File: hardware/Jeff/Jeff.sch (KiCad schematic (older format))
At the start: 1 part

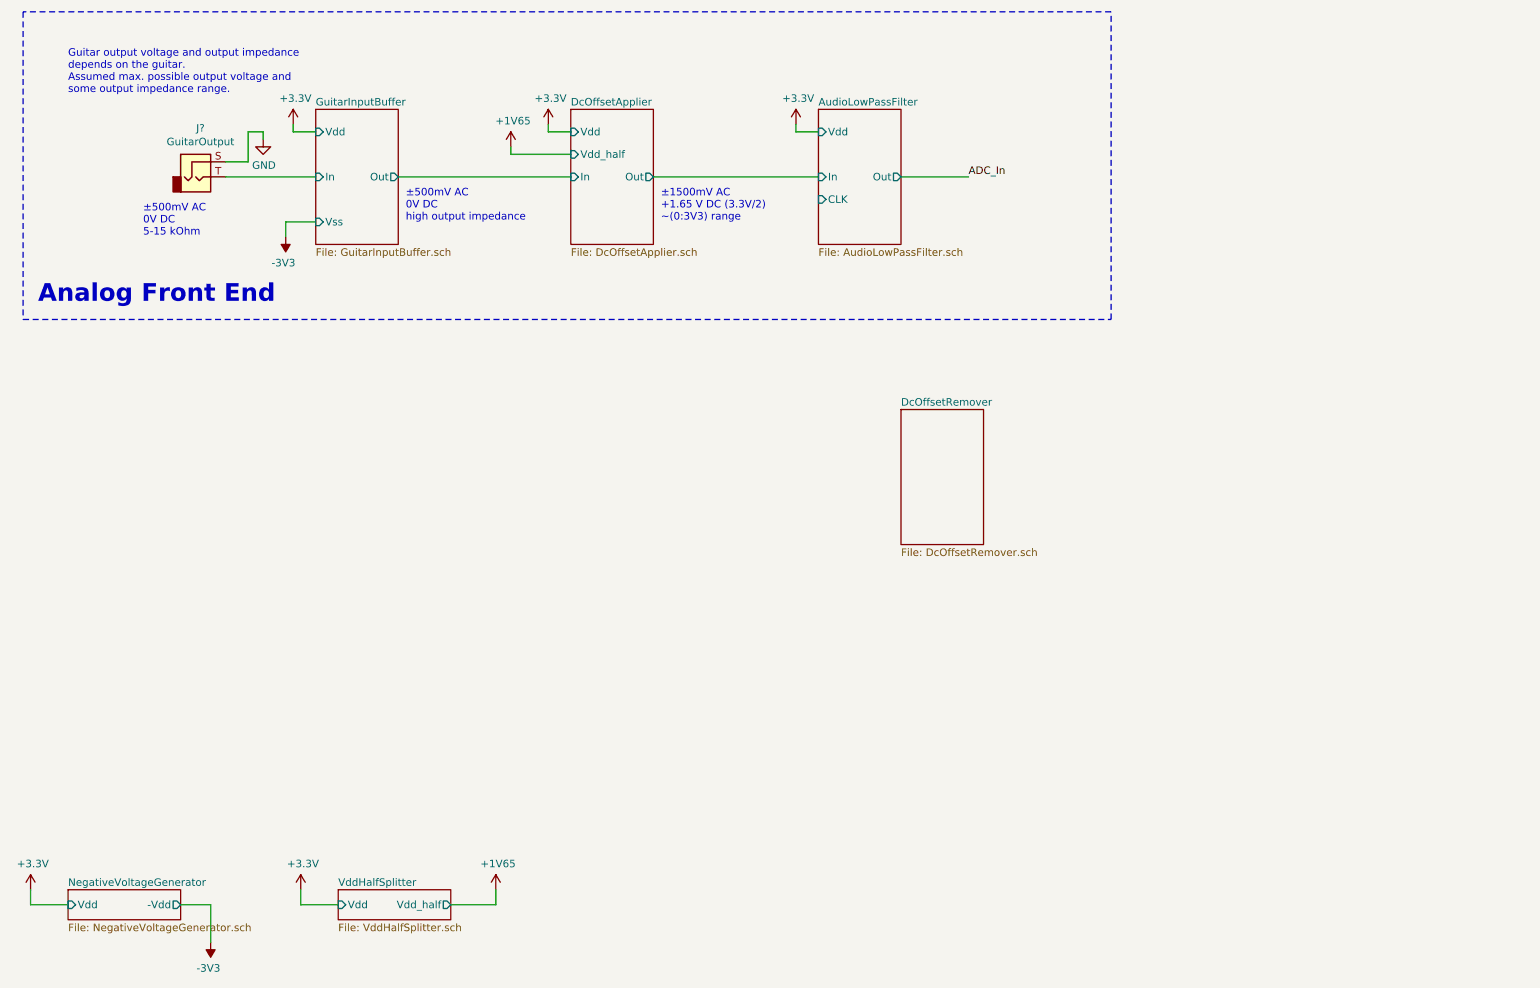
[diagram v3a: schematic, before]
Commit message: Add DSP block and connect to analog front end
The DSP block contains STM32L432KC nucleo board, which is also added
with this commit, as a library. The output of the analog front end has
been connected to the CPU as well as the cutoff frequency setter clock.
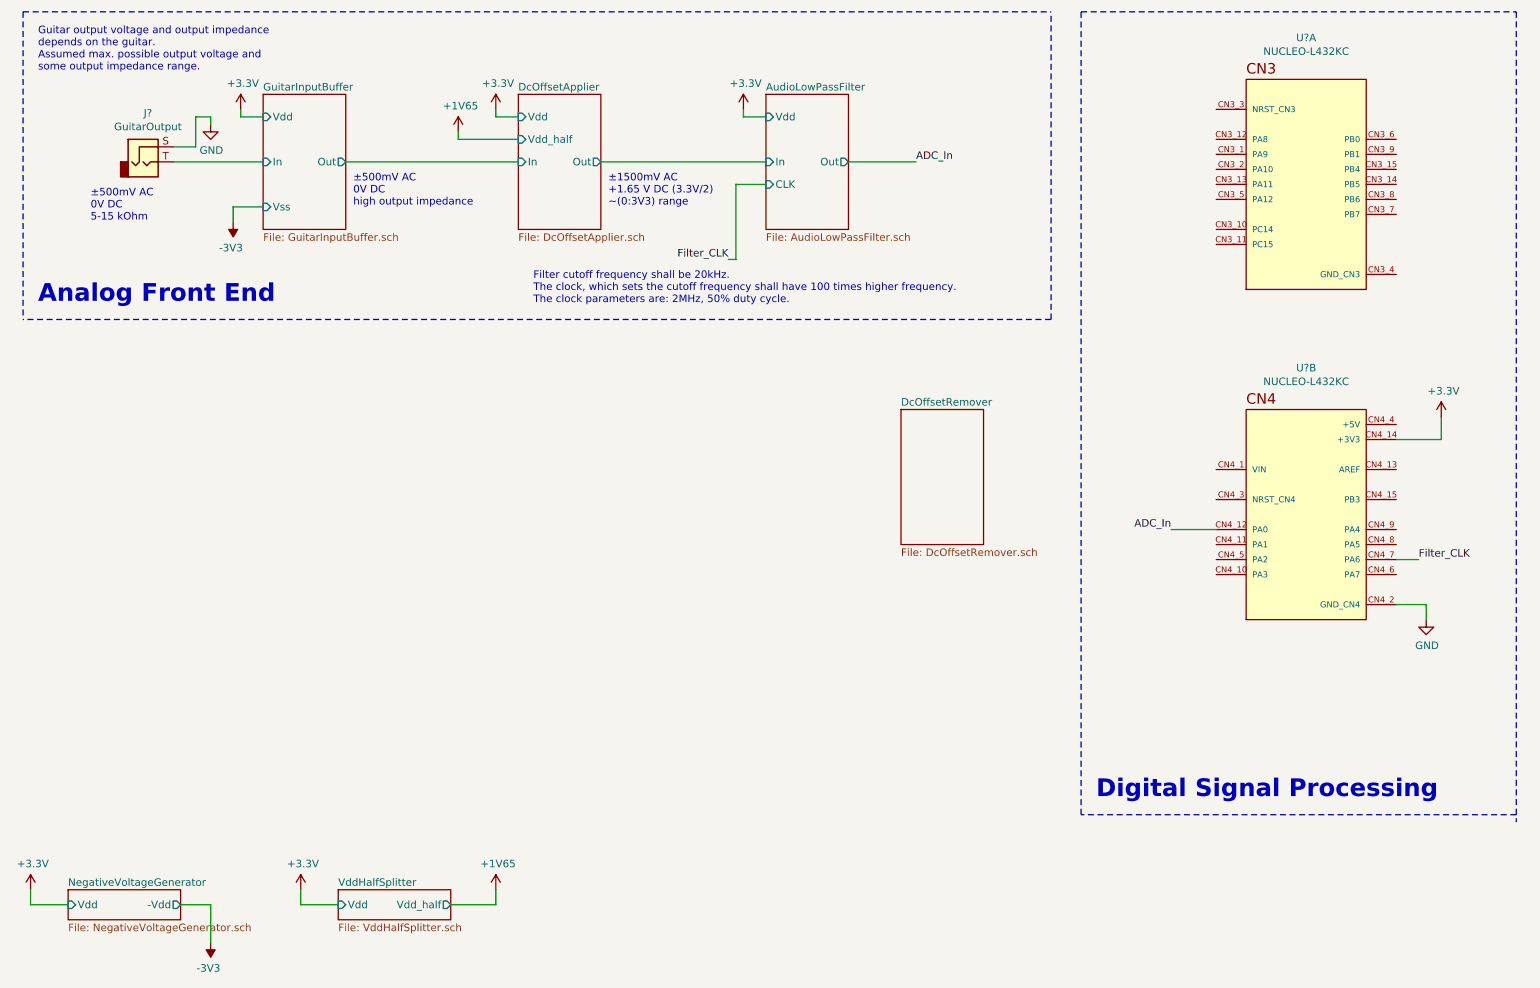
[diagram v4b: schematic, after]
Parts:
- added U? (x2): NUCLEO-L432KC, MODULE_NUCLEO-L432KC, symbol Nucleo-L432KC:NUCLEO-L432KC
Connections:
- net +3V3: now also U?.CN4_14 (+3V3)
- net ADC_In: now also U?.CN4_12 (PA0)
- net GND: now also U?.CN4_2 (GND_CN4)
- new net Filter_CLK: U?.CN4_7 (PA6)
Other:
- note added: "Digital Signal Processing"
- note added: "Filter cutoff frequency shall be 20kHz.\nThe clock, which sets the cutoff frequency shall have 100 times higher frequency.\nThe clock parameters are: 2MHz, 50% duty cycle."
- moved on the sheet: J?

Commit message: Add Post-DAC stage schematic
This includes the low pass filter, which is the same like the one in the
Front End, the offset remover circuit, all the connections to DSP stage,
which is the DAC output and the filter cutoff setter clock.
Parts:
- added J?: JeffOutput, symbol Connector:AudioJack2
- J?: value GuitarOutput -> Guitar
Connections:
- net GND: now also J?.S
- net DAC_Out: now reaches U?.CN4_9 (PA4)
- new net DcOffsetRemover/Out: J?.T
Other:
- note added: "Miscellanuous"
- note added: "Post-DAC Stage"
- note added: "±1650mV AC\n0V DC"
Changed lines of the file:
@@
 $Descr A4 11693 8268
 encoding utf-8
-Sheet 1 7
+Sheet 1 8
 Title ""
 Date ""
@@
 P 1800 1800
 F 0 "J?" H 1832 2125 50  0000 C CNN
-F 1 "GuitarOutput" H 1832 2034 50  0000 C CNN
+F 1 "Guitar" H 1832 2034 50  0000 C CNN
 F 2 "" H 1800 1800 50  0001 C CNN
 F 3 "~" H 1800 1800 50  0001 C CNN
@@
 Wire Wire Line
 	2250 1500 2150 1500
-$Sheet
-S 6850 3450 550  900
-U 6216C0D1
-F0 "DcOffsetRemover" 50
-F1 "DcOffsetRemover.sch" 50
-$EndSheet
 Text Notes 1450 2200 0    50   ~ 0
 ±500mV AC\n0V DC\n5-15 kOhm
@@
 	5800 1500 5800 1450
 $Sheet
-S 1300 6650 750  200
+S 2100 6000 750  200
 U 6219438A
 F0 "NegativeVoltageGenerator" 50
 F1 "NegativeVoltageGenerator.sch" 50
-F2 "Vdd" I L 1300 6750 50
-F3 "-Vdd" O R 2050 6750 50
+F2 "Vdd" I L 2100 6100 50
+F3 "-Vdd" O R 2850 6100 50
 $EndSheet
 $Comp
 L power:+3.3V #PWR?
 U 1 1 6219F15D
-P 1050 6650
-F 0 "#PWR?" H 1050 6500 50  0001 C CNN
-F 1 "+3.3V" H 1065 6823 50  0000 C CNN
-F 2 "" H 1050 6650 50  0001 C CNN
-F 3 "" H 1050 6650 50  0001 C CNN
-	1    1050 6650
-	1    0    0    -1
-$EndComp
-Wire Wire Line
-	1300 6750 1050 6750
-Wire Wire Line
-	1050 6750 1050 6650
+P 1850 6000
+F 0 "#PWR?" H 1850 5850 50  0001 C CNN
+F 1 "+3.3V" H 1865 6173 50  0000 C CNN
+F 2 "" H 1850 6000 50  0001 C CNN
+F 3 "" H 1850 6000 50  0001 C CNN
+	1    1850 6000
+	1    0    0    -1
+$EndComp
+Wire Wire Line
+	2100 6100 1850 6100
+Wire Wire Line
+	1850 6100 1850 6000
 $Comp
 L power:-3V3 #PWR?
 U 1 1 6219FAA4
-P 2250 7000
-F 0 "#PWR?" H 2250 7100 50  0001 C CNN
-F 1 "-3V3" H 2265 7173 50  0000 C CNN
-F 2 "" H 2250 7000 50  0001 C CNN
-F 3 "" H 2250 7000 50  0001 C CNN
-	1    2250 7000
+P 3050 6350
+F 0 "#PWR?" H 3050 6450 50  0001 C CNN
+F 1 "-3V3" H 3065 6523 50  0000 C CNN
+F 2 "" H 3050 6350 50  0001 C CNN
+F 3 "" H 3050 6350 50  0001 C CNN
+	1    3050 6350
 	-1   0    0    1
 $EndComp
 Wire Wire Line
-	2050 6750 2250 6750
-Wire Wire Line
-	2250 6750 2250 7000
+	2850 6100 3050 6100
+Wire Wire Line
+	3050 6100 3050 6350
 $Comp
 L power:-3V3 #PWR?
@@
 	2400 2100 2400 2200
 $Sheet
-S 3100 6650 750  200
+S 3900 6000 750  200
 U 621A29F4
 F0 "VddHalfSplitter" 50
 F1 "VddHalfSplitter.sch" 50
-F2 "Vdd" I L 3100 6750 50
-F3 "Vdd_half" O R 3850 6750 50
+F2 "Vdd" I L 3900 6100 50
+F3 "Vdd_half" O R 4650 6100 50
 $EndSheet
 $Comp
 L power:+3.3V #PWR?
 U 1 1 621A9A4A
-P 2850 6650
-F 0 "#PWR?" H 2850 6500 50  0001 C CNN
-F 1 "+3.3V" H 2865 6823 50  0000 C CNN
-F 2 "" H 2850 6650 50  0001 C CNN
-F 3 "" H 2850 6650 50  0001 C CNN
-	1    2850 6650
-	1    0    0    -1
-$EndComp
-Wire Wire Line
-	3100 6750 2850 6750
-Wire Wire Line
-	2850 6750 2850 6650
+P 3650 6000
+F 0 "#PWR?" H 3650 5850 50  0001 C CNN
+F 1 "+3.3V" H 3665 6173 50  0000 C CNN
+F 2 "" H 3650 6000 50  0001 C CNN
+F 3 "" H 3650 6000 50  0001 C CNN
+	1    3650 6000
+	1    0    0    -1
+$EndComp
+Wire Wire Line
+	3900 6100 3650 6100
+Wire Wire Line
+	3650 6100 3650 6000
 $Comp
 L PowerSources:+1V65 #PWR?
 U 1 1 621AA734
-P 4150 6650
-F 0 "#PWR?" H 4150 6500 50  0001 C CNN
-F 1 "+1V65" H 4165 6823 50  0000 C CNN
-F 2 "" H 4150 6650 50  0001 C CNN
-F 3 "" H 4150 6650 50  0001 C CNN
-	1    4150 6650
-	1    0    0    -1
-$EndComp
-Wire Wire Line
-	4150 6650 4150 6750
-Wire Wire Line
-	4150 6750 3850 6750
+P 4950 6000
+F 0 "#PWR?" H 4950 5850 50  0001 C CNN
+F 1 "+1V65" H 4965 6173 50  0000 C CNN
+F 2 "" H 4950 6000 50  0001 C CNN
+F 3 "" H 4950 6000 50  0001 C CNN
+	1    4950 6000
+	1    0    0    -1
+$EndComp
+Wire Wire Line
+	4950 6000 4950 6100
+Wire Wire Line
+	4950 6100 4650 6100
 $Comp
 L PowerSources:+1V65 #PWR?
@@
 Text Notes 4400 2750 0    50   ~ 0
 Filter cutoff frequency shall be 20kHz.\nThe clock, which sets the cutoff frequency shall have 100 times higher frequency.\nThe clock parameters are: 2MHz, 50% duty cycle.
+$Sheet
+S 2950 3450 550  900
+U 621EA432
+F0 "Post-DAC filter" 50
+F1 "AudioLowPassFilter.sch" 50
+F2 "Vdd" I L 2950 3600 50
+F3 "In" I L 2950 3900 50
+F4 "CLK" I L 2950 4050 50
+F5 "Out" O R 3500 3900 50
+$EndSheet
+$Sheet
+S 4700 3450 550  900
+U 6216C0D1
+F0 "DcOffsetRemover" 50
+F1 "DcOffsetRemover.sch" 50
+F2 "Vdd_half" I L 4700 3750 50
+F3 "In" I L 4700 3900 50
+F4 "Out" O R 5250 3900 50
+F5 "Vss" I L 4700 4200 50
+F6 "Vdd" I L 4700 3600 50
+$EndSheet
+Wire Wire Line
+	2950 3900 2050 3900
+Text Label 2050 3900 2    50   ~ 0
+DAC_Out
+Text Notes 1950 4200 0    50   ~ 0
+±1500mV AC\n+1.65 V DC (3.3V/2)\n~~(0:3V3) range
+$Comp
+L power:+3.3V #PWR?
+U 1 1 621F8F58
+P 2800 3550
+F 0 "#PWR?" H 2800 3400 50  0001 C CNN
+F 1 "+3.3V" H 2815 3723 50  0000 C CNN
+F 2 "" H 2800 3550 50  0001 C CNN
+F 3 "" H 2800 3550 50  0001 C CNN
+	1    2800 3550
+	1    0    0    -1
+$EndComp
+Wire Wire Line
+	2950 3600 2800 3600
+Wire Wire Line
+	2800 3600 2800 3550
+Text Label 2650 4400 2    50   ~ 0
+Filter_CLK
+Wire Wire Line
+	2850 4400 2850 4050
+Wire Wire Line
+	2850 4050 2950 4050
+Wire Wire Line
+	2650 4400 2850 4400
+$Comp
+L power:+3.3V #PWR?
+U 1 1 622055E0
+P 4550 3550
+F 0 "#PWR?" H 4550 3400 50  0001 C CNN
+F 1 "+3.3V" H 4565 3723 50  0000 C CNN
+F 2 "" H 4550 3550 50  0001 C CNN
+F 3 "" H 4550 3550 50  0001 C CNN
+	1    4550 3550
+	1    0    0    -1
+$EndComp
+Wire Wire Line
+	4700 3600 4550 3600
+Wire Wire Line
+	4550 3600 4550 3550
+$Comp
+L power:-3V3 #PWR?
+U 1 1 62206B7F
+P 4500 4300
+F 0 "#PWR?" H 4500 4400 50  0001 C CNN
+F 1 "-3V3" H 4515 4473 50  0000 C CNN
+F 2 "" H 4500 4300 50  0001 C CNN
+F 3 "" H 4500 4300 50  0001 C CNN
+	1    4500 4300
+	-1   0    0    1
+$EndComp
+Wire Wire Line
+	4700 4200 4500 4200
+Wire Wire Line
+	4500 4200 4500 4300
+Wire Wire Line
+	3500 3900 4700 3900
+Text Notes 3550 4200 0    50   ~ 0
+±1500mV AC\n+1.65 V DC (3.3V/2)\n~~(0:3V3) range
+$Comp
+L PowerSources:+1V65 #PWR?
+U 1 1 6220A05A
+P 4300 3700
+F 0 "#PWR?" H 4300 3550 50  0001 C CNN
+F 1 "+1V65" H 4315 3873 50  0000 C CNN
+F 2 "" H 4300 3700 50  0001 C CNN
+F 3 "" H 4300 3700 50  0001 C CNN
+	1    4300 3700
+	1    0    0    -1
+$EndComp
+Wire Wire Line
+	4300 3700 4300 3750
+Wire Wire Line
+	4700 3750 4300 3750
+$Comp
+L Connector:AudioJack2 J?
+U 1 1 6220C08B
+P 6500 3900
+F 0 "J?" H 6532 4225 50  0000 C CNN
+F 1 "JeffOutput" H 6532 4134 50  0000 C CNN
+F 2 "" H 6500 3900 50  0001 C CNN
+F 3 "~" H 6500 3900 50  0001 C CNN
+	1    6500 3900
+	-1   0    0    -1
+$EndComp
+$Comp
+L power:GND #PWR?
+U 1 1 62210BD7
+P 6050 3650
+F 0 "#PWR?" H 6050 3400 50  0001 C CNN
+F 1 "GND" H 6055 3477 50  0000 C CNN
+F 2 "" H 6050 3650 50  0001 C CNN
+F 3 "" H 6050 3650 50  0001 C CNN
+	1    6050 3650
+	-1   0    0    -1
+$EndComp
+Wire Wire Line
+	6300 3800 6150 3800
+Wire Wire Line
+	6150 3800 6150 3600
+Wire Wire Line
+	6050 3650 6050 3600
+Wire Wire Line
+	6050 3600 6150 3600
+Wire Wire Line
+	6300 3900 5250 3900
+Text Notes 5300 4100 0    50   ~ 0
+±1650mV AC\n0V DC
+Wire Notes Line
+	1000 3050 7850 3050
+Wire Notes Line
+	7850 3050 7850 4950
+Wire Notes Line
+	7850 4950 1000 4950
+Wire Notes Line
+	1000 4950 1000 3050
+Text Notes 1100 4850 0    118  ~ 24
+Post-DAC Stage
+Wire Notes Line
+	1000 5200 1000 7000
+Wire Notes Line
+	1000 7000 5800 7000
+Wire Notes Line
+	5800 7000 5800 5200
+Wire Notes Line
+	5800 5200 1000 5200
+Text Notes 1150 6850 0    118  ~ 24
+Miscellanuous
+Wire Wire Line
+	10150 4250 10300 4250
+Text Label 10300 4250 0    50   ~ 0
+DAC_Out
 $EndSCHEMATC
